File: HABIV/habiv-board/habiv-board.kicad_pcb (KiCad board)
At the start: 4 copper layers, 100.3 x 120.9 mm, 129 parts, among them IC1 RTC_PCF8523T, J1 Micro_SD_Card_Det, J10 Conn_01x02_Female, J11 Conn_01x02_Female, J12 Conn_01x02_Female, J13 Conn_01x02_Female, J14 Conn_01x02_Female, J15 Conn_01x02_Female, J16 Conn_01x02_Female, J17 Conn_01x03_Male, J18 Conn_01x03_Male, J19 Conn_01x03_Male, J2 Conn_ARM_JTAG_SWD_20, J20 Conn_01x05_Male, J21 Conn_01x04_Male, J22 Conn_01x04_Male, J3 Conn_01x02_Male, J4 Conn_01x16_Male, J6 Conn_01x16_Male, J7 Conn_01x16_Male, J8 Conn_01x02_Female, J9 Conn_01x02_Male, Q1 32.768KHz, SW1 SW_DPST_x2, U1 STM32F401RET6, U2 MAX31855, U3 FGPMMOPA6H, U4 TPS564208, U5 TPS564208, U7 MS560702BA03-00, Y1 32.768MHz

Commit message: Updates for rn
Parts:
- removed C21: 10u, Capacitor_SMD:C_0805_2012Metric
- removed J17: Conn_01x03_Male, Connector_PinHeader_2.54mm:PinHeader_1x03_P2.54mm_Vertical
- removed the LED1 at (42.4, 66.0)
- removed R16: 1K, Resistor_SMD:R_0805_2012Metric
- removed the R23 at (51.4, 63.5)
- removed R44: 0, Resistor_SMD:R_0805_2012Metric
- added JP6: Jumper, Connector_PinHeader_2.54mm:PinHeader_1x02_P2.54mm_Vertical, F.Cu at (167.1, 38.2)
- moved J22 10.2 mm to (154.7, 49.0), turned to 180 degrees
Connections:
- IC1 pad 8: Net-(IC1-Pad8) -> Net-(C4-Pad1)
- R2 pad 1: Net-(IC1-Pad8) -> +3V3
- R3 pad 1: Net-(IC1-Pad8) -> +3V3
- U3 pad P$13: (no net) -> Net-(U3-PadP$13)
- U3 pad P$14: (no net) -> Net-(U3-PadP$14)
- U3 pad P$15: (no net) -> Net-(U3-PadP$15)
- U3 pad P$16: (no net) -> Net-(U3-PadP$16)
- U3 pad P$17: (no net) -> Net-(U3-PadP$17)
- U3 pad P$18: (no net) -> Net-(U3-PadP$18)
- U3 pad P$2: (no net) -> Net-(U3-PadP$2)
- U3 pad P$20: (no net) -> Net-(U3-PadP$20)
- U3 pad P$4: (no net) -> Net-(U3-PadP$4)
- U3 pad P$6: (no net) -> Net-(U3-PadP$6)
- U3 pad P$7: (no net) -> Net-(U3-PadP$7)
- U7 pad 1: Net-(R44-Pad2) -> Net-(C10-Pad1)
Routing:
- net Net-(JP6-Pad1): track 0.00 -> 9.47 mm
- net Net-(C1-Pad1): track 6.49 -> 0.00 mm, vias 2 -> 0
- net PB8: track 118.7 -> 124.4 mm
- net Net-(IC1-Pad8): track 13.5 -> 8.16 mm
- net +3V3: track 71.8 -> 67.2 mm, vias 13 -> 14
- net Net-(R44-Pad2): track 1.90 -> 0.00 mm
- net Net-(C10-Pad1): track 12.3 -> 13.4 mm, vias 1 -> 0

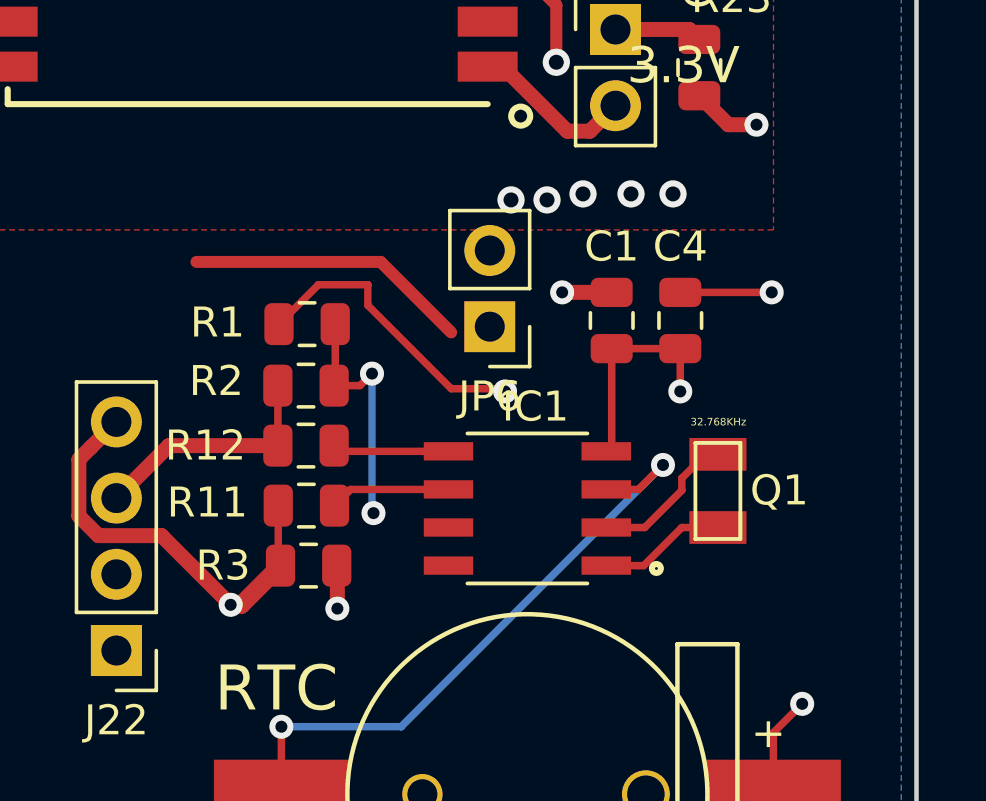
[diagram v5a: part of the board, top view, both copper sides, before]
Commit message: JP on RTC
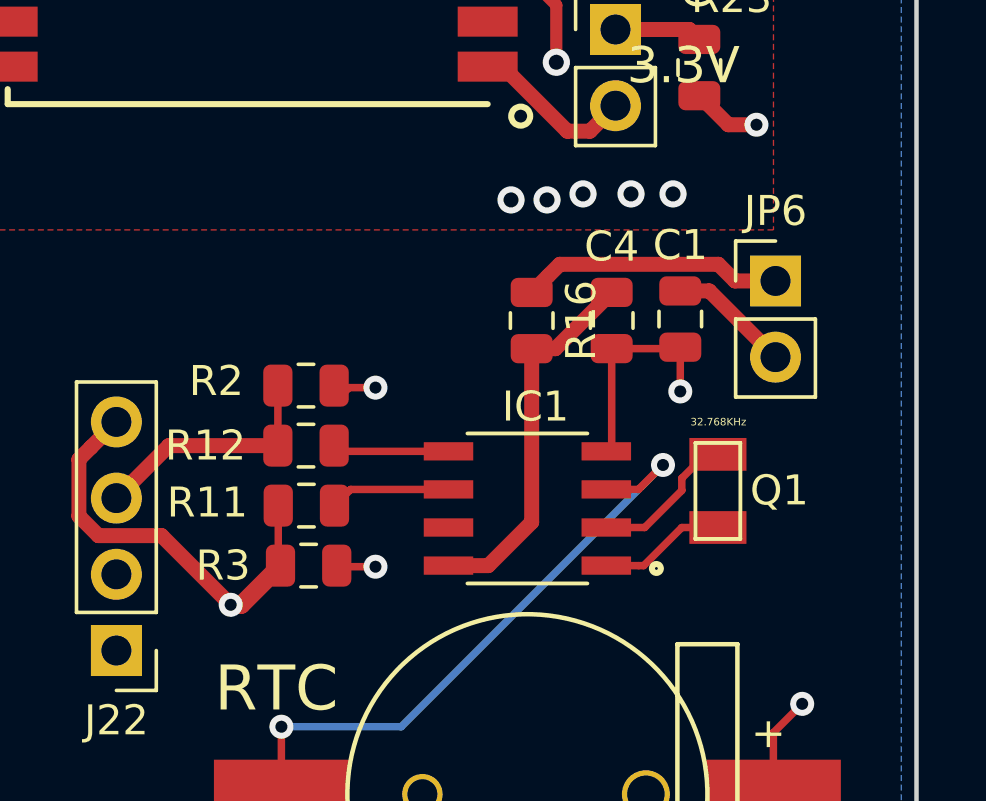
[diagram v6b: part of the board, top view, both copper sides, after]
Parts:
- removed R1: 0, Resistor_SMD:R_0805_2012Metric
- added R16: 1K, Resistor_SMD:R_0805_2012Metric, F.Cu at (168.5, 38.0)
- C4: value 10u -> 3.3uF
- moved JP6 9.65 mm to (176.7, 36.7), turned to 0 degrees
- moved C1 2.29 mm to (173.5, 38.0)
- moved C4 2.29 mm to (171.2, 38.0)
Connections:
- JP6 pad 1: Net-(C4-Pad1) -> Net-(JP6-Pad1)
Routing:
- net Net-(C4-Pad1): track 23.6 -> 13.0 mm, vias 2 -> 0
- net Net-(IC1-Pad8): track 8.16 -> 0.00 mm, vias 2 -> 0
- net +3V3: track 67.2 -> 70.9 mm
- net Net-(JP6-Pad1): track 9.47 -> 8.75 mm

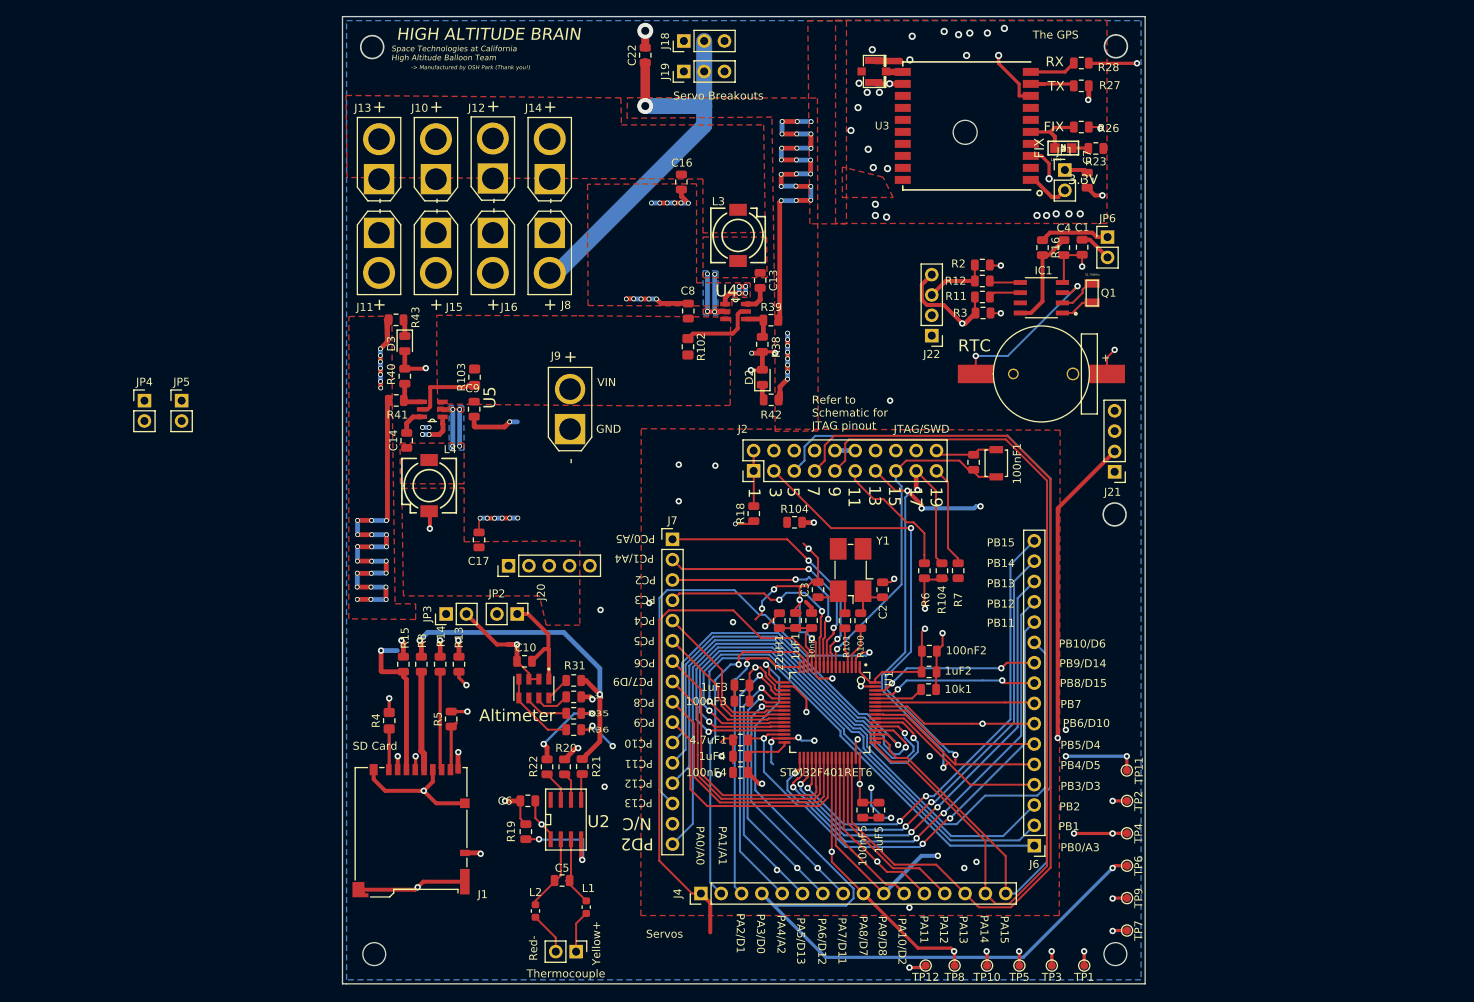
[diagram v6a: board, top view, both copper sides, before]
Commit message: Added all jumpers
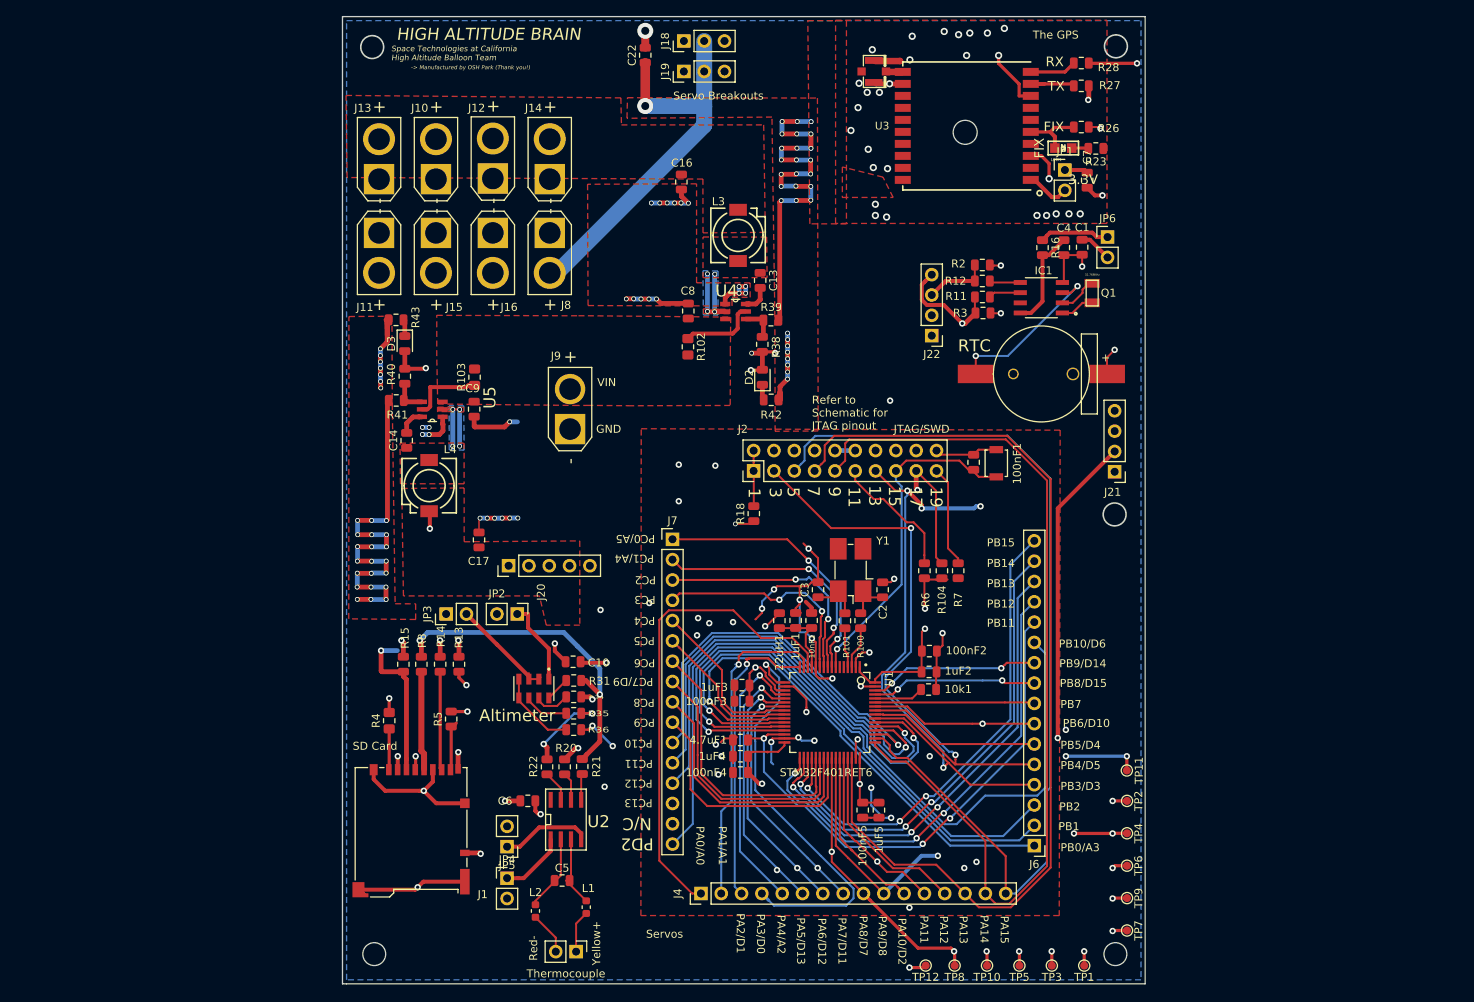
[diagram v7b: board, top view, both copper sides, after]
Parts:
- removed the R104 at (137.5, 72.4)
- removed R19: 0, Resistor_SMD:R_0805_2012Metric
- moved JP4 75.0 mm to (101.6, 116.8)
- moved JP5 69.0 mm to (101.6, 112.9), turned to 180 degrees
- moved C10 6.08 mm to (109.9, 89.8), turned to 0 degrees
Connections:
- C10 pad 1: Net-(C10-Pad1) -> +3V3
- C10 pad 2: Net-(C10-Pad2) -> GND
- C6 pad 1: Net-(C6-Pad1) -> GND
- C6 pad 2: Net-(C6-Pad2) -> +3V3
- JP2 pad 1: Net-(C10-Pad1) -> Net-(JP2-Pad1)
- JP3 pad 2: Net-(C10-Pad2) -> Net-(JP3-Pad2)
- JP4 pad 1: Net-(C6-Pad2) -> Net-(JP4-Pad1)
- JP5 pad 1: Net-(C6-Pad1) -> Net-(JP5-Pad1)
- U2 pad 1: Net-(C6-Pad2) -> Net-(JP4-Pad1)
- U2 pad 4: Net-(R19-Pad2) -> Net-(JP5-Pad1)
- U7 pad 1: Net-(C10-Pad1) -> Net-(JP2-Pad1)
- U7 pad 2: Net-(C10-Pad2) -> Net-(JP3-Pad2)
- U7 pad 3: Net-(C10-Pad2) -> Net-(JP3-Pad2)
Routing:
- net PC3: track 112.1 -> 67.8 mm
- net Net-(C10-Pad2): track 15.6 -> 0.00 mm, vias 1 -> 0
- net Net-(JP3-Pad2): track 0.00 -> 13.7 mm
- net Net-(C10-Pad1): track 13.4 -> 0.00 mm
- net Net-(R19-Pad2): track 12.3 -> 0.00 mm, vias 2 -> 0
- net Net-(JP5-Pad1): track 0.00 -> 11.4 mm
- net Net-(JP2-Pad1): track 0.00 -> 10.7 mm
- net PC13: track 59.7 -> 49.3 mm, vias 1 -> 2
- net PA3: track 167.2 -> 176.0 mm
- net Net-(JP4-Pad1): track 0.00 -> 8.34 mm
- net Net-(C6-Pad2): track 5.60 -> 0.00 mm, vias 1 -> 0
- net PA0: track 65.4 -> 60.0 mm
- net GND: track 330.1 -> 335.3 mm, vias 139 -> 144
- net Net-(C6-Pad1): track 5.12 -> 0.00 mm, vias 1 -> 0
- net +3V3: track 70.9 -> 75.6 mm, vias 14 -> 16
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
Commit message: double checked
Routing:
- net PA15: track 119.5 -> 93.3 mm
- net Net-(J2-Pad17): track 30.1 -> 12.9 mm, vias 1 -> 0
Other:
- board text removed: "FIX"
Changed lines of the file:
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@@
   (general
     (thickness 1.6)
-    (drawings 93)
-    (tracks 1811)
+    (drawings 91)
+    (tracks 1801)
     (zones 0)
     (modules 122)
@@
     (1 In1.Cu power hide)
     (2 In2.Cu signal hide)
-    (31 B.Cu signal)
+    (31 B.Cu signal hide)
     (32 B.Adhes user hide)
-    (33 F.Adhes user hide)
+    (33 F.Adhes user)
     (34 B.Paste user hide)
     (35 F.Paste user hide)
     (36 B.SilkS user)
-    (37 F.SilkS user)
+    (37 F.SilkS user hide)
     (38 B.Mask user)
     (39 F.Mask user)
@@
     (effects (font (size 1.5 1.5) (thickness 0.3)))
   )
-  (gr_text FIX (at 168.656 23.622) (layer F.SilkS)
-    (effects (font (size 1.2065 1.2065) (thickness 0.1905)) (justify left bottom))
-  )
   (gr_text 3.3V (at 171.704 30.226) (layer F.SilkS)
     (effects (font (size 1.2065 1.2065) (thickness 0.1905)) (justify left bottom))
@@
     (effects (font (size 1.2065 1.2065) (thickness 0.1905)) (justify left bottom mirror))
   )
-  (gr_text FIX (at 168.8416 26.8729 90) (layer F.SilkS)
-    (effects (font (size 1.2065 1.2065) (thickness 0.1905)) (justify left bottom))
-  )
   (gr_text RTC (at 160.02 50.292) (layer F.SilkS)
     (effects (font (size 1.5 1.5) (thickness 0.15)))
@@
   (segment (start 152.091788 73.084937) (end 152.091788 88.520425) (width 0.25) (layer B.Cu) (net 23))
   (segment (start 179.07 103.378) (end 179.07 101.6) (width 0.4) (layer F.Cu) (net 23))
-  (segment (start 179.07 101.6) (end 171.45 101.6) (width 0.4) (layer B.Cu) (net 23))
   (segment (start 171.45 101.6) (end 171.45 101.6) (width 0.4) (layer B.Cu) (net 23))
   (via (at 171.45 101.6) (size 0.8) (drill 0.4) (layers F.Cu B.Cu) (net 23))
   (segment (start 168.514975 101.6) (end 167.500727 102.614248) (width 0.4) (layer In1.Cu) (net 23))
   (segment (start 171.45 101.6) (end 168.514975 101.6) (width 0.4) (layer In1.Cu) (net 23))
-  (segment (start 163.929487 118.758488) (end 165.131568 118.758488) (width 0.25) (layer B.Cu) (net 24) (status 10))
-  (segment (start 164.137767 61.517048) (end 164.102207 61.552608) (width 0.25) (layer B.Cu) (net 24))
-  (segment (start 165.131568 118.758488) (end 169.065367 114.824689) (width 0.25) (layer B.Cu) (net 24))
-  (segment (start 169.065367 114.824689) (end 169.065367 105.96502) (width 0.25) (layer B.Cu) (net 24))
-  (segment (start 169.510297 105.52009) (end 169.510297 66.889578) (width 0.25) (layer B.Cu) (net 24))
-  (segment (start 169.065367 105.96502) (end 169.510297 105.52009) (width 0.25) (layer B.Cu) (net 24))
-  (segment (start 169.510297 66.889578) (end 164.137767 61.517048) (width 0.25) (layer B.Cu) (net 24))
-  (segment (start 164.102207 61.552608) (end 140.138205 61.552608) (width 0.25) (layer B.Cu) (net 24))
-  (segment (start 140.138205 61.552608) (end 138.782651 62.908162) (width 0.25) (layer B.Cu) (net 24))
-  (segment (start 138.782651 62.908162) (end 138.782651 64.647164) (width 0.25) (layer B.Cu) (net 24))
-  (segment (start 138.782651 64.647164) (end 138.348246 65.081569) (width 0.25) (layer B.Cu) (net 24) (status 20))
-  (segment (start 138.348246 65.081569) (end 137.498247 65.931568) (width 0.25) (layer B.Cu) (net 24) (status 30))
   (segment (start 163.929487 117.556407) (end 163.929487 118.758488) (width 0.25) (layer F.Cu) (net 24) (status 20))
   (segment (start 149.421765 100.93645) (end 150.298765 101.81345) (width 0.25) (layer F.Cu) (net 24))
@@
   (segment (start 151.546615 72.359936) (end 152.414789 72.359936) (width 0.25) (layer F.Cu) (net 103))
   (segment (start 153.764407 73.709554) (end 153.764407 76.463128) (width 0.25) (layer F.Cu) (net 103))
-  (via (at 152.908 68.326) (size 0.8) (drill 0.4) (layers F.Cu B.Cu) (net 104))
   (segment (start 152.738247 65.931568) (end 155.222367 68.415688) (width 0.25) (layer F.Cu) (net 104) (status 10))
-  (segment (start 152.738247 68.156247) (end 152.908 68.326) (width 0.6) (layer F.Cu) (net 104))
-  (segment (start 152.738247 65.931568) (end 152.738247 68.156247) (width 0.6) (layer F.Cu) (net 104))
   (segment (start 155.222367 76.741995) (end 155.956 77.475628) (width 0.25) (layer F.Cu) (net 104))
   (segment (start 155.222367 68.415688) (end 155.222367 76.741995) (width 0.25) (layer F.Cu) (net 104))
-  (segment (start 152.508001 68.873985) (end 152.508001 68.725999) (width 0.6) (layer In2.Cu) (net 104))
-  (segment (start 152.073778 69.308208) (end 152.508001 68.873985) (width 0.6) (layer In2.Cu) (net 104))
-  (segment (start 152.508001 68.725999) (end 152.908 68.326) (width 0.6) (layer In2.Cu) (net 104))
-  (segment (start 143.035792 69.308208) (end 152.073778 69.308208) (width 0.6) (layer In2.Cu) (net 104))
-  (segment (start 139.954 72.39) (end 143.035792 69.308208) (width 0.6) (layer In2.Cu) (net 104))
   (segment (start 155.278247 65.931568) (end 156.665087 67.318408) (width 0.25) (layer F.Cu) (net 105) (status 10))
   (segment (start 157.988 76.8825) (end 156.718 75.6125) (width 0.25) (layer F.Cu) (net 105))
@@
   (segment (start 114.808 101.732643) (end 114.808 100.895685) (width 0.3) (layer In2.Cu) (net 10))
   (segment (start 142.188167 113.538) (end 137.351376 108.701209) (width 0.3) (layer In2.Cu) (net 10))
+  (segment (start 172.015685 101.6) (end 179.07 101.6) (width 0.4) (layer F.Cu) (net 23))
+  (segment (start 171.45 101.6) (end 172.015685 101.6) (width 0.4) (layer F.Cu) (net 23))
+  (segment (start 137.498247 70.31893) (end 137.498247 67.133649) (width 0.25) (layer In2.Cu) (net 24))
+  (segment (start 137.498247 67.133649) (end 137.498247 65.931568) (width 0.25) (layer In2.Cu) (net 24))
+  (segment (start 158.074999 115.245999) (end 158.325592 114.995406) (width 0.25) (layer In2.Cu) (net 24))
+  (segment (start 158.325592 114.995406) (end 158.325592 91.146275) (width 0.25) (layer In2.Cu) (net 24))
+  (segment (start 158.074999 115.894001) (end 158.074999 115.245999) (width 0.25) (layer In2.Cu) (net 24))
+  (segment (start 159.814485 117.633487) (end 158.074999 115.894001) (width 0.25) (layer In2.Cu) (net 24))
+  (segment (start 158.325592 91.146275) (end 137.498247 70.31893) (width 0.25) (layer In2.Cu) (net 24))
+  (segment (start 162.804486 117.633487) (end 159.814485 117.633487) (width 0.25) (layer In2.Cu) (net 24))
+  (segment (start 163.929487 118.758488) (end 162.804486 117.633487) (width 0.25) (layer In2.Cu) (net 24))
   (segment (start 128.369487 113.819513) (end 128.397 113.792) (width 0.25) (layer B.Cu) (net 30))
   (segment (start 128.369487 118.758488) (end 128.369487 113.819513) (width 0.25) (layer B.Cu) (net 30))
